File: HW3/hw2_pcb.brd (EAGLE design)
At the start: 50 x 50 mm, 22 parts, among them J1 USB-MB-H

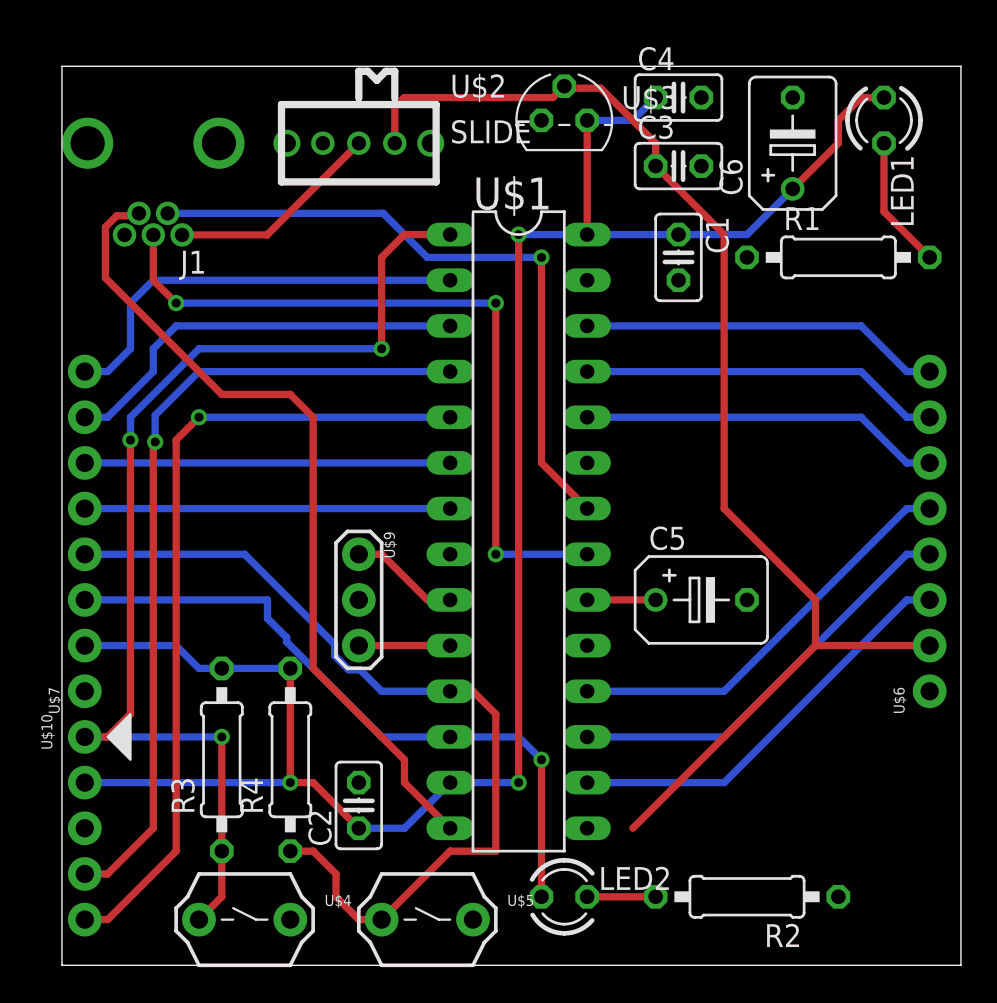
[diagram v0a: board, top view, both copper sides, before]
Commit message: Added copper plane for GND connections
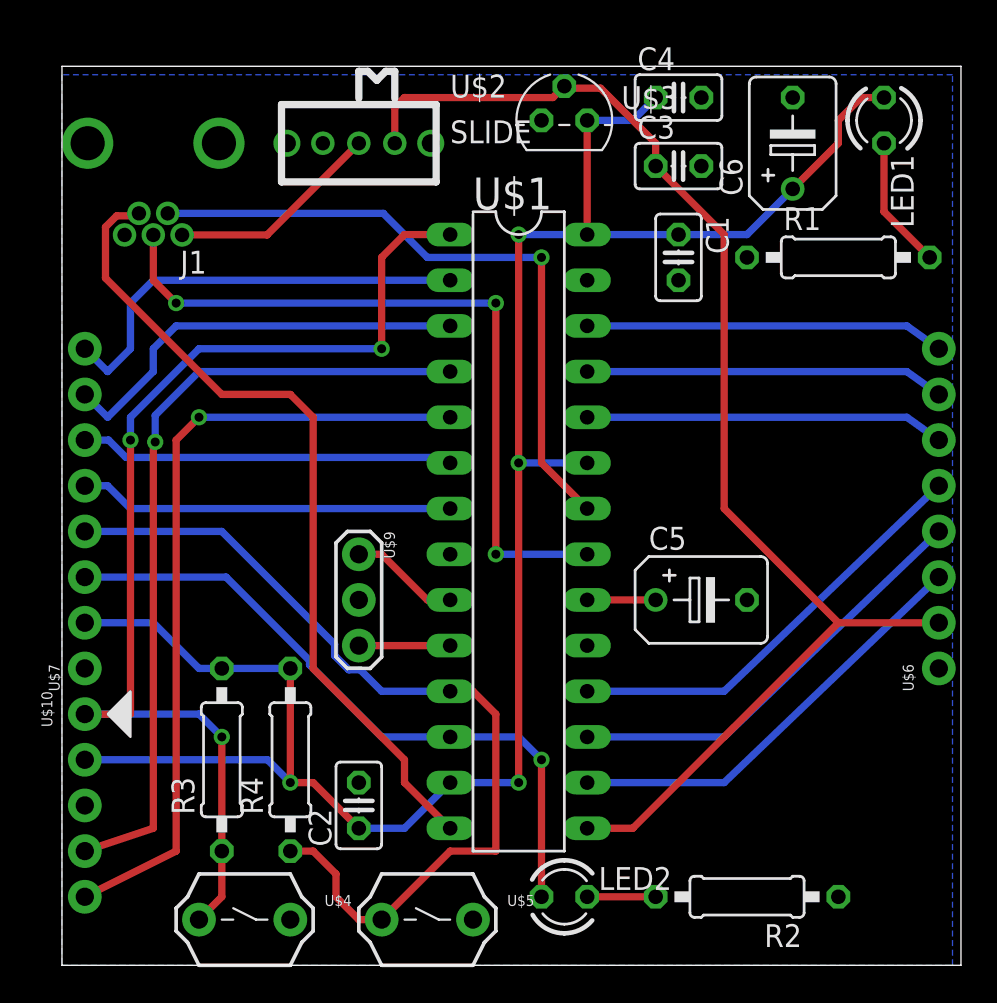
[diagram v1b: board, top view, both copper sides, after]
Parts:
- moved U$6 1.37 mm to (48.8, 16.5)
- moved U$10 1.27 mm to (1.27, 14.0)
- moved U$7 1.27 mm to (1.27, 16.5)
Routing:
- net +3V3: track 109.9 -> 114.8 mm, vias 3 -> 4
- net +5V: track 70.6 -> 73.4 mm
- net PGC: track 45.3 -> 44.3 mm
- net B9: track 23.3 -> 24.1 mm
- net B8: track 23.3 -> 24.1 mm
- net B7: track 23.3 -> 24.1 mm
- net PGD: track 45.5 -> 44.6 mm
- net B3: track 20.3 -> 20.8 mm
- net A1: track 23.2 -> 23.7 mm
- net B2: track 20.3 -> 20.8 mm
- net A0: track 23.9 -> 24.4 mm
- net B4/USER: track 49.9 -> 50.4 mm
- added copper zone on layer 16, net GND

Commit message: UI board updates. Still working on this.
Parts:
- renumbered U$1 to U1, U$2 to U2, U$3 to U3, U$5 to U5, U$9 to U9
